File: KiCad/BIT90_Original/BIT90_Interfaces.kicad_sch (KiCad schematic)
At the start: 7 parts, among them CN1a KO, CN1b KI, CN2 Cartridge, CN3 Expansion

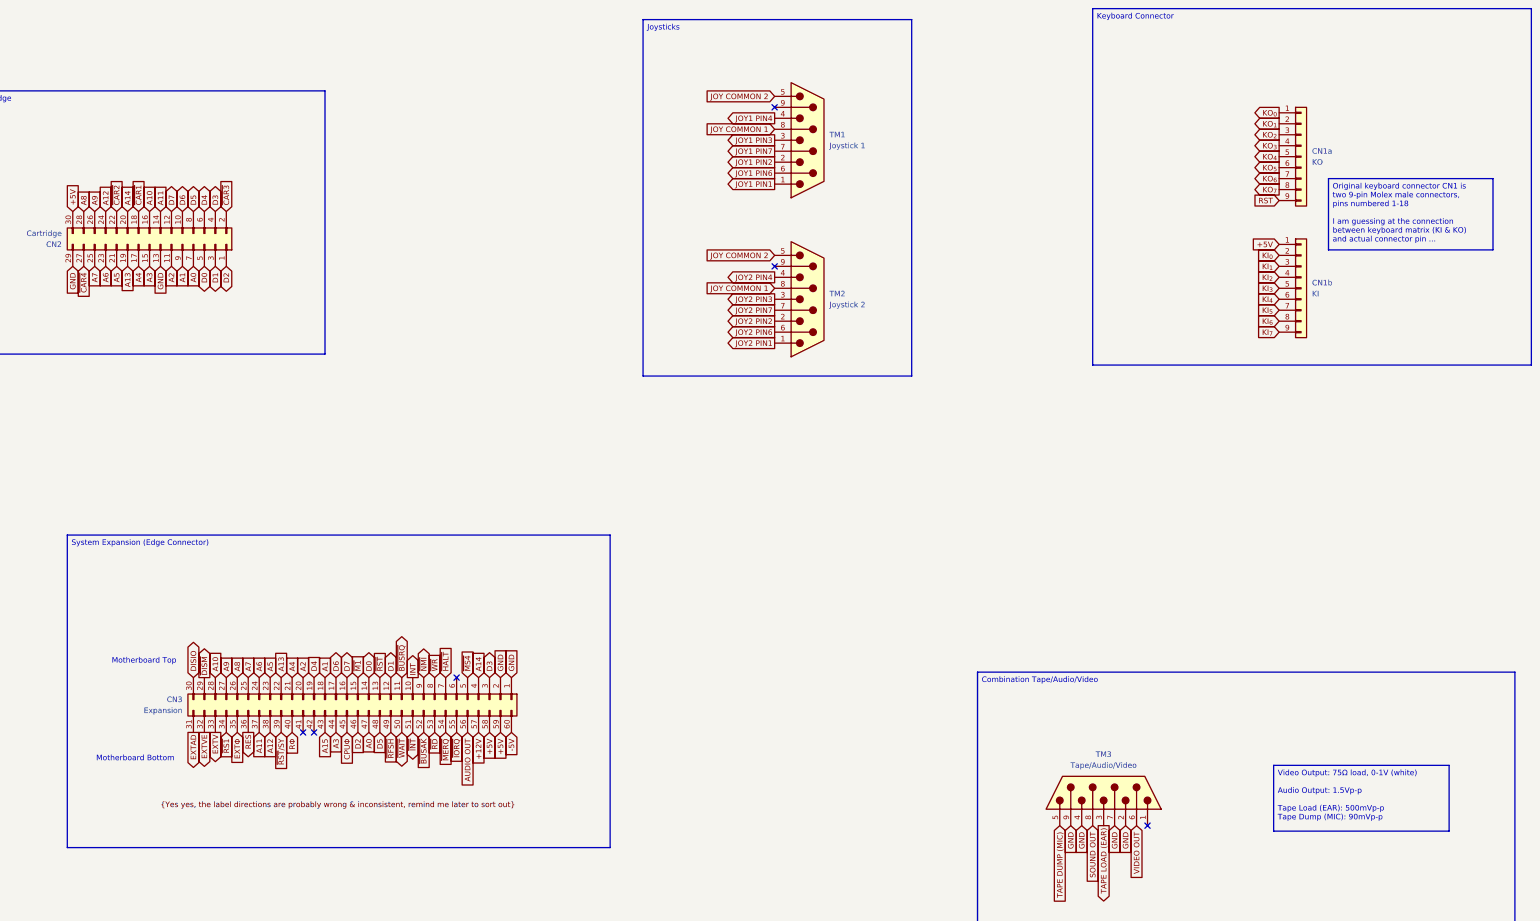
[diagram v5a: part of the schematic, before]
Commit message: Small updates/corrections
Managed to figure out some more errors/missing info from ColecoVision schematics & Henk's BIT90 motherboard underside photo
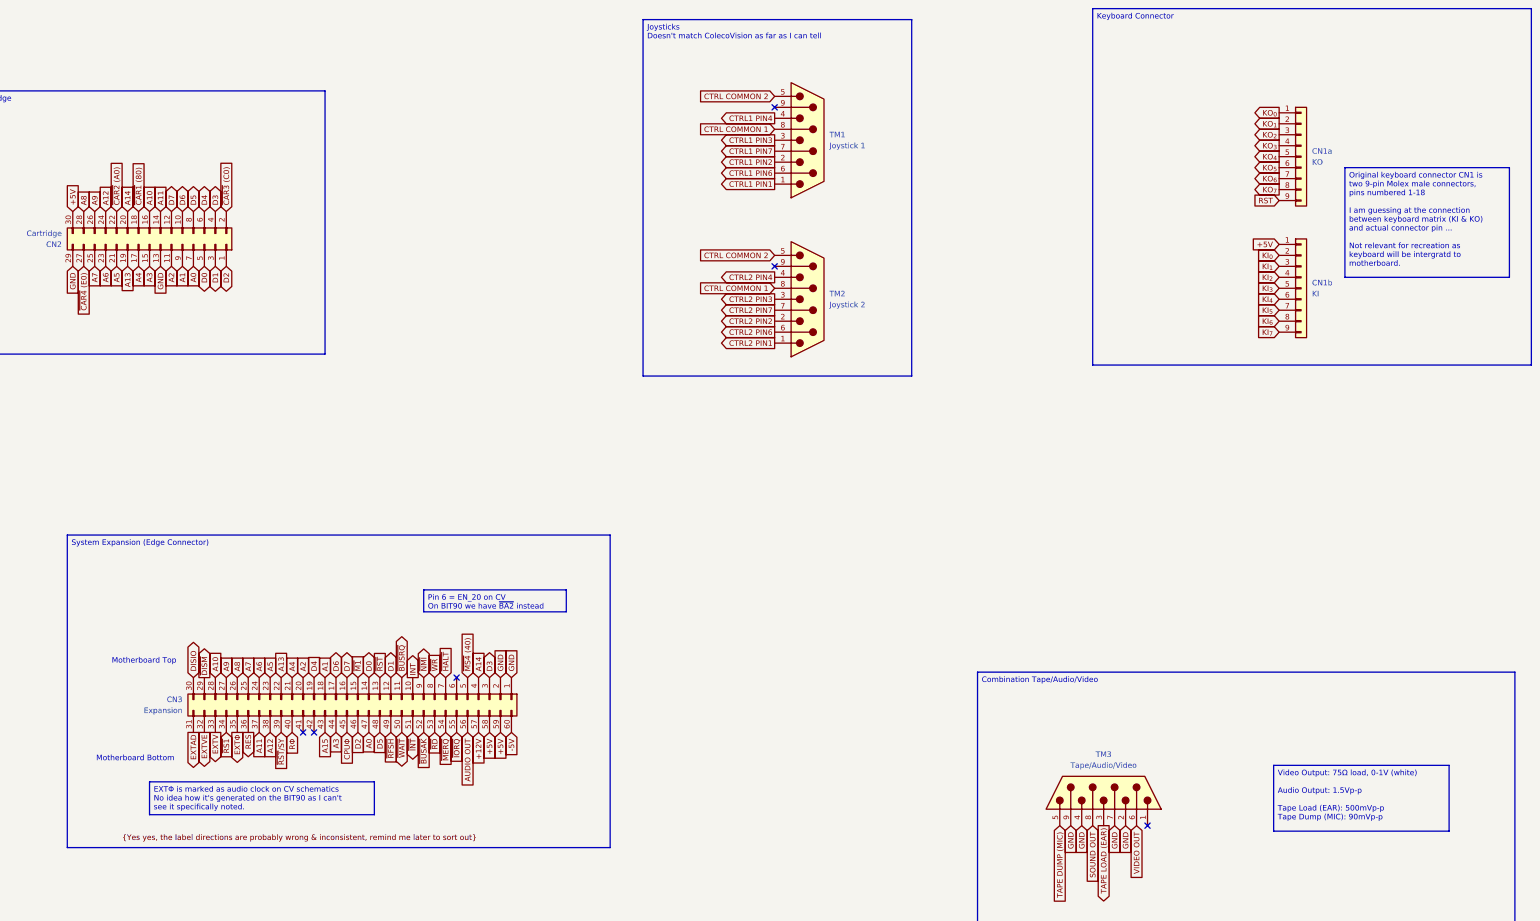
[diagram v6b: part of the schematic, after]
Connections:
- net JOY COMMON 1 renamed CTRL COMMON 1
- net JOY COMMON 2 renamed CTRL COMMON 2
- net JOY1 PIN1 renamed CTRL1 PIN1
- net JOY1 PIN2 renamed CTRL1 PIN2
- net JOY1 PIN3 renamed CTRL1 PIN3
- net JOY1 PIN4 renamed CTRL1 PIN4
- net JOY1 PIN6 renamed CTRL1 PIN6
- net JOY1 PIN7 renamed CTRL1 PIN7
- net JOY2 PIN1 renamed CTRL2 PIN1
- net JOY2 PIN2 renamed CTRL2 PIN2
- net JOY2 PIN3 renamed CTRL2 PIN3
- net JOY2 PIN4 renamed CTRL2 PIN4
- net JOY2 PIN6 renamed CTRL2 PIN6
- net JOY2 PIN7 renamed CTRL2 PIN7
- net ~{CAR1} renamed ~{CAR1} (80)
- net ~{CAR2} renamed ~{CAR2} (A0)
- net ~{CAR3} renamed ~{CAR3} (C0)
- net ~{CAR4} renamed ~{CAR4} (E0)
- net ~{MS4} renamed ~{MS4} (40)
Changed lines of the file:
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@@
 	(title_block
 		(title "BIT90 Interfaces")
-		(date "3/JUN/2026")
+		(date "5/JUN/2026")
 		(rev "A")
 		(company "Brett Hallen")
@@
 		)
 	)
+	(text_box "EXTΦ is marked as audio clock on CV schematics\nNo idea how it's generated on the BIT90 as I can't see it specifically noted."
+		(exclude_from_sim no)
+		(at 77.47 201.93 0)
+		(size 52.07 7.62)
+		(margins 0.9525 0.9525 0.9525 0.9525)
+		(stroke
+			(width 0)
+			(type solid)
+		)
+		(fill
+			(type none)
+		)
+		(effects
+			(font
+				(size 1.27 1.27)
+				(thickness 0.1588)
+			)
+			(justify left top)
+		)
+	)
 	(text_box "System Expansion (Edge Connector)"
 		(exclude_from_sim no)
@@
 		)
 	)
-	(text_box "Joysticks"
+	(text_box "Joysticks\nDoesn't match ColecoVision as far as I can tell"
 		(exclude_from_sim no)
 		(at 191.77 25.4 0)
@@
 		)
 	)
-	(text_box "Original keyboard connector CN1 is two 9-pin Molex male connectors, pins numbered 1-18\n\nI am guessing at the connection between keyboard matrix (KI & KO) and actual connector pin ..."
+	(text_box "Pin 6 = EN_20 on CV\nOn BIT90 we have ~{BA2} instead"
 		(exclude_from_sim no)
-		(at 350.52 62.23 0)
-		(size 38.1 16.51)
+		(at 140.97 157.48 0)
+		(size 33.02 5.08)
 		(margins 0.9525 0.9525 0.9525 0.9525)
 		(stroke
@@
 		)
 	)
+	(text_box "Original keyboard connector CN1 is two 9-pin Molex male connectors, pins numbered 1-18\n\nI am guessing at the connection between keyboard matrix (KI & KO) and actual connector pin ...\n\nNot relevant for recreation as keyboard will be intergratd to motherboard."
+		(exclude_from_sim no)
+		(at 354.33 59.69 0)
+		(size 38.1 25.4)
+		(margins 0.9525 0.9525 0.9525 0.9525)
+		(stroke
+			(width 0)
+			(type solid)
+		)
+		(fill
+			(type none)
+		)
+		(effects
+			(font
+				(size 1.27 1.27)
+			)
+			(justify left top)
+		)
+	)
 	(no_connect
 		(at 222.25 45.72)
@@
 	)
 	(label "{Yes yes, the label directions are probably wrong & inconsistent, remind me later to sort out}"
-		(at 80.01 208.28 0)
+		(at 71.12 215.9 0)
 		(effects
 			(font
@@
 		)
 	)
-	(global_label "~{CAR2}"
+	(global_label "~{CAR2} (A0)"
 		(shape input)
 		(at 69.85 69.85 90)
@@
 		)
 	)
-	(global_label "JOY2 PIN6"
+	(global_label "CTRL2 PIN6"
 		(shape output)
 		(at 222.25 97.79 180)
@@
 		)
 	)
-	(global_label "JOY1 PIN2"
+	(global_label "CTRL1 PIN2"
 		(shape output)
 		(at 222.25 58.42 180)
@@
 		)
 	)
-	(global_label "JOY2 PIN1"
+	(global_label "CTRL2 PIN1"
 		(shape output)
 		(at 222.25 100.33 180)
@@
 		)
 	)
-	(global_label "JOY2 PIN7"
+	(global_label "CTRL2 PIN7"
 		(shape output)
 		(at 222.25 92.71 180)
@@
 		)
 	)
-	(global_label "JOY COMMON 1"
+	(global_label "CTRL COMMON 1"
 		(shape input)
 		(at 222.25 50.8 180)
@@
 		)
 	)
-	(global_label "JOY1 PIN7"
+	(global_label "CTRL1 PIN7"
 		(shape output)
 		(at 222.25 55.88 180)
@@
 		)
 	)
-	(global_label "JOY COMMON 1"
+	(global_label "CTRL COMMON 1"
 		(shape input)
 		(at 222.25 87.63 180)
@@
 	)
 	(global_label "EXTΦ"
-		(shape input)
+		(shape output)
 		(at 97.79 190.5 270)
 		(fields_autoplaced yes)
@@
 		)
 	)
-	(global_label "JOY1 PIN4"
+	(global_label "CTRL1 PIN4"
 		(shape output)
 		(at 222.25 48.26 180)
@@
 		)
 	)
-	(global_label "JOY2 PIN4"
+	(global_label "CTRL2 PIN4"
 		(shape output)
 		(at 222.25 85.09 180)
@@
 		)
 	)
-	(global_label "JOY COMMON 2"
+	(global_label "CTRL COMMON 2"
 		(shape input)
 		(at 222.25 80.01 180)
@@
 		)
 	)
-	(global_label "JOY COMMON 2"
+	(global_label "CTRL COMMON 2"
 		(shape input)
 		(at 222.25 43.18 180)
@@
 		)
 	)
-	(global_label "~{MS4}"
+	(global_label "~{MS4} (40)"
 		(shape input)
 		(at 151.13 177.8 90)
@@
 		)
 	)
-	(global_label "JOY2 PIN2"
+	(global_label "CTRL2 PIN2"
 		(shape output)
 		(at 222.25 95.25 180)
@@
 		)
 	)
-	(global_label "JOY1 PIN6"
+	(global_label "CTRL1 PIN6"
 		(shape output)
 		(at 222.25 60.96 180)
@@
 		)
 	)
-	(global_label "JOY2 PIN3"
+	(global_label "CTRL2 PIN3"
 		(shape output)
 		(at 222.25 90.17 180)
@@
 		)
 	)
-	(global_label "~{CAR4}"
+	(global_label "~{CAR4} (E0)"
 		(shape input)
 		(at 62.23 82.55 270)
@@
 		)
 	)
-	(global_label "~{CAR3}"
+	(global_label "~{CAR3} (C0)"
 		(shape input)
 		(at 95.25 69.85 90)
@@
 		)
 	)
-	(global_label "JOY1 PIN1"
+	(global_label "CTRL1 PIN1"
 		(shape output)
 		(at 222.25 63.5 180)
@@
 		)
 	)
-	(global_label "JOY1 PIN3"
+	(global_label "CTRL1 PIN3"
 		(shape output)
 		(at 222.25 53.34 180)
@@
 		)
 	)
-	(global_label "~{CAR1}"
+	(global_label "~{CAR1} (80)"
 		(shape input)
 		(at 74.93 69.85 90)

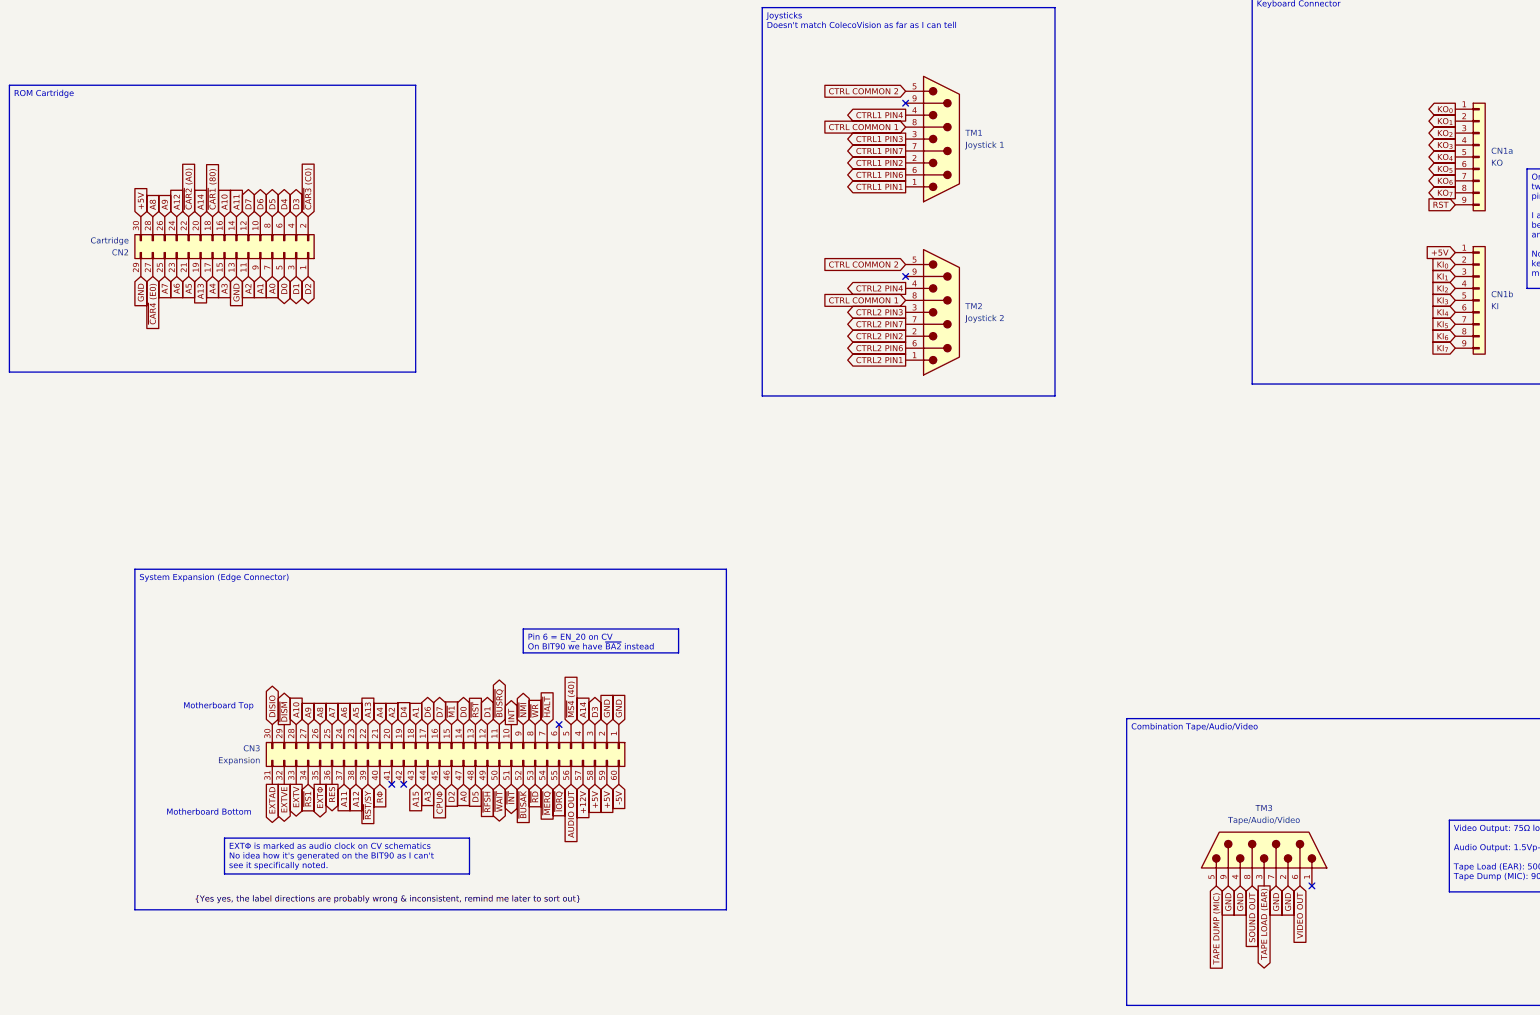
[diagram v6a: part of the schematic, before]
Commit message: Resolved audio clock signal
Marked as EXTΦ on BIT90 schematic, generated via resistor from CPUΦ
Renamed it as AUDΦ so it's a bit clearer
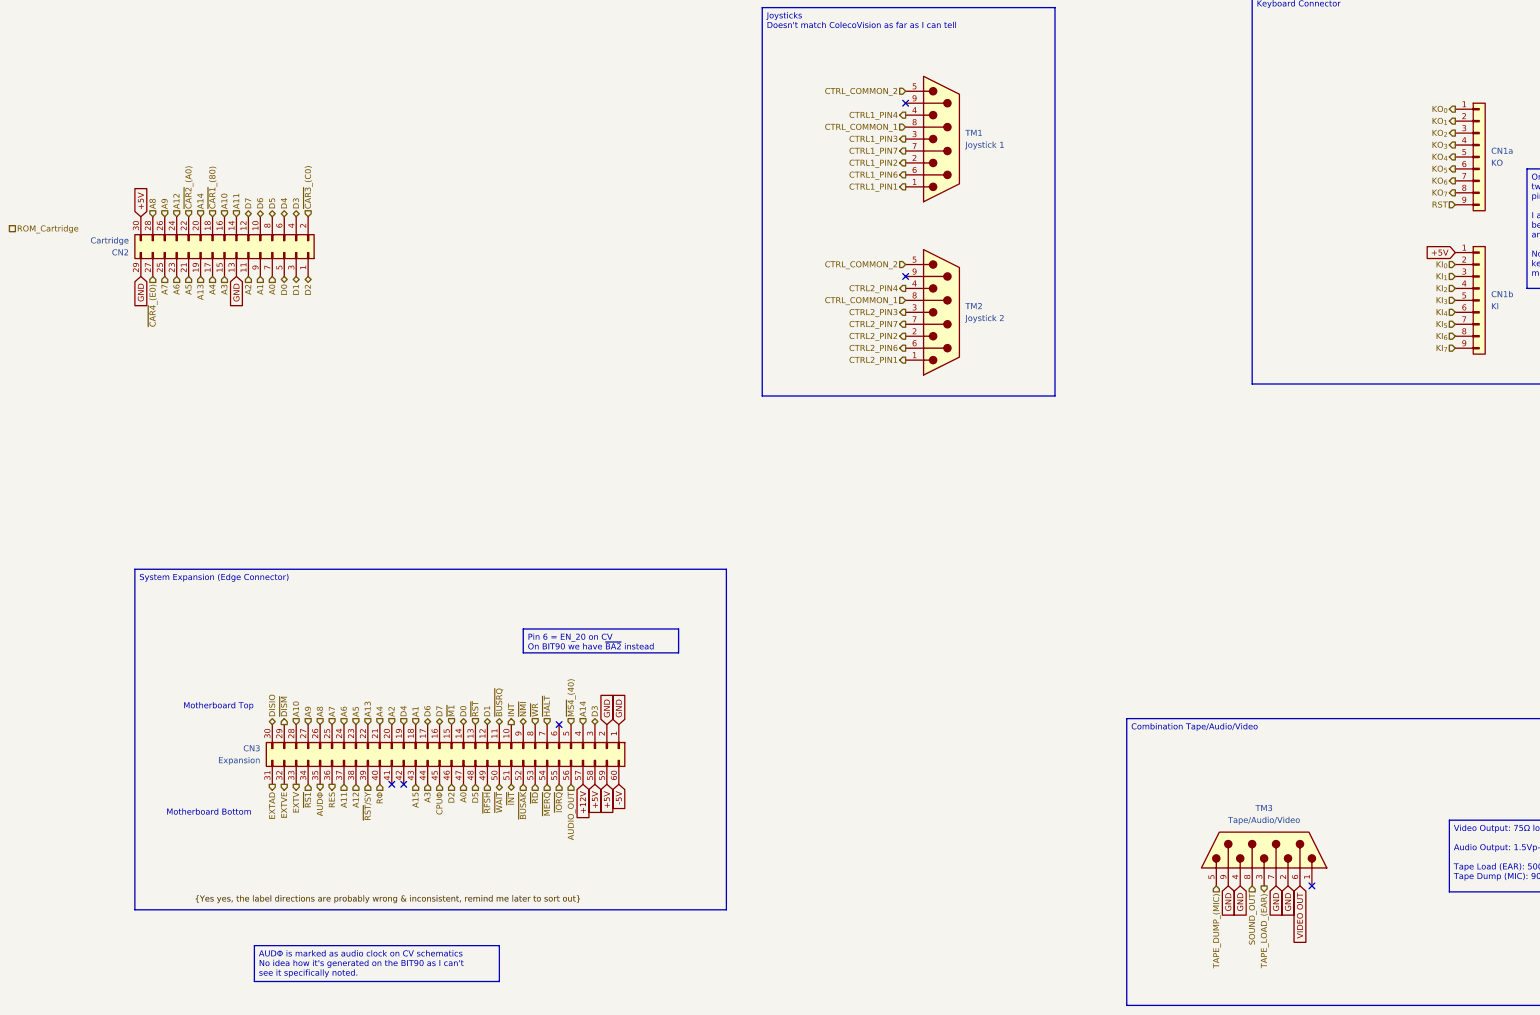
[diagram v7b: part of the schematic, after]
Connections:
- net AUDIO OUT renamed AUDIO_OUT
- net CTRL COMMON 1 renamed CTRL_COMMON_1
- net CTRL COMMON 2 renamed CTRL_COMMON_2
- net CTRL1 PIN1 renamed CTRL1_PIN1
- net CTRL1 PIN2 renamed CTRL1_PIN2
- net CTRL1 PIN3 renamed CTRL1_PIN3
- net CTRL1 PIN4 renamed CTRL1_PIN4
- net CTRL1 PIN6 renamed CTRL1_PIN6
- net CTRL1 PIN7 renamed CTRL1_PIN7
- net CTRL2 PIN1 renamed CTRL2_PIN1
- net CTRL2 PIN2 renamed CTRL2_PIN2
- net CTRL2 PIN3 renamed CTRL2_PIN3
- net CTRL2 PIN4 renamed CTRL2_PIN4
- net CTRL2 PIN6 renamed CTRL2_PIN6
- net CTRL2 PIN7 renamed CTRL2_PIN7
- net EXTΦ renamed AUDΦ
- net SOUND OUT renamed SOUND_OUT
- net TAPE DUMP (MIC) renamed TAPE_DUMP_(MIC)
- net TAPE LOAD (EAR) renamed TAPE_LOAD_(EAR)
- net ~{CAR1} (80) renamed ~{CAR1}_(80)
- net ~{CAR2} (A0) renamed ~{CAR2}_(A0)
- net ~{CAR3} (C0) renamed ~{CAR3}_(C0)
- net ~{CAR4} (E0) renamed ~{CAR4}_(E0)
- net ~{MS4} (40) renamed ~{MS4}_(40)

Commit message: Minor corrections
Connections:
- net DISIO renamed ~{DISIO}
